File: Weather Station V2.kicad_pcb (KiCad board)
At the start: 4 copper layers, 123.5 x 67.3 mm, 66 parts, among them J1 SOLAR IN, J10 SP13 Socket, J2 18650, J3 Battery_AUX, J4 Conn_01x08_Socket, J5 Conn_01x08_Socket, J6 USB_C, J7 RYLR998, J8 Breakout, J9 SP13 Socket, Q1 AO4842, Q2 DMP2240UDM-7, Q3 BC547, SW1 LED_ENABLE, SW2 EN/RST, SW3 BOOT, SW4 POWER_SELECT, SW6 POWER, U1 TP4056, U2 DW01A, U3 LDL1117S33R, U4 MT3608, U5 ESP32-S3-WROOM-1U, U7 USBLC6-2SC6

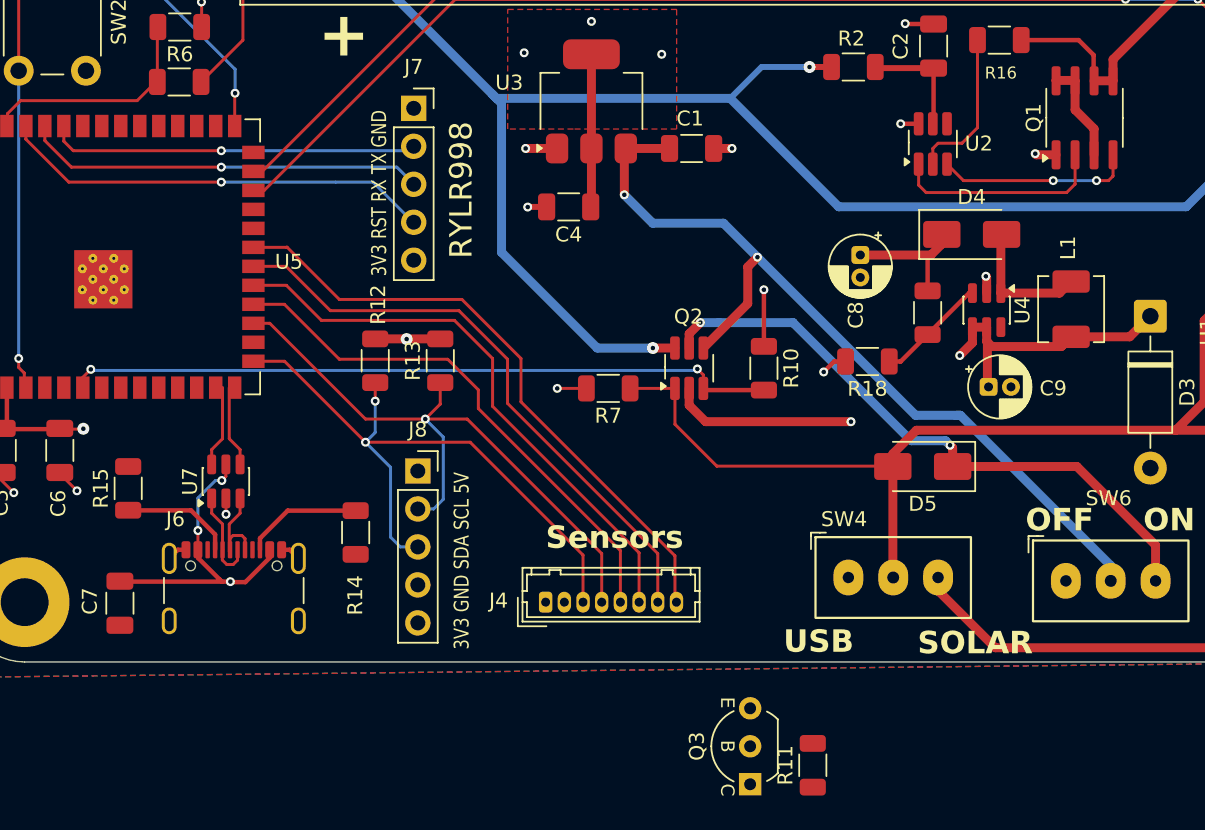
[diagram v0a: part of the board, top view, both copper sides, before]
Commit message: - Connected open collector mosfet driver to 5V reg - Re-routed tracks related to NMOS
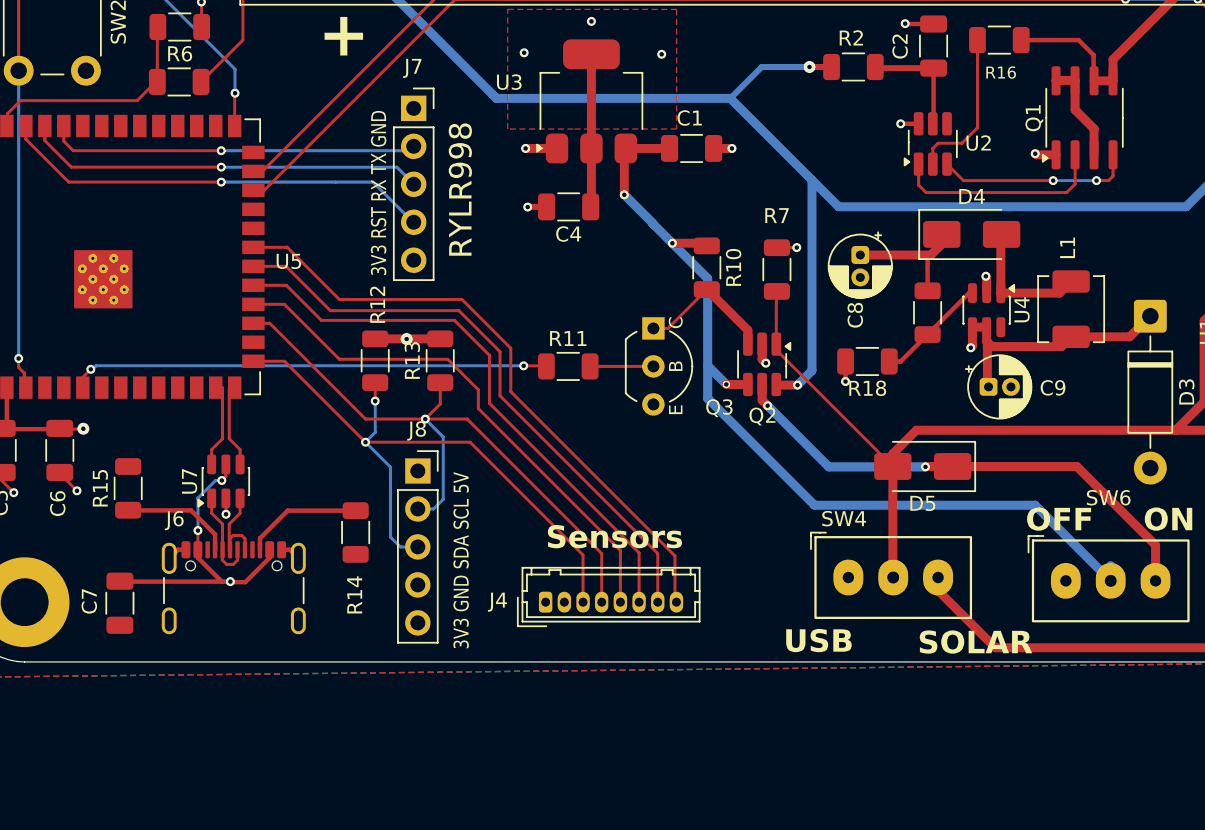
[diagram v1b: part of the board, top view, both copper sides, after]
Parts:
- moved R11 31.3 mm to (128.8, 105.2), turned to 0 degrees
- moved Q3 31.2 mm to (134.5, 102.6), turned to -90 degrees
- moved R7 13.8 mm to (142.8, 98.7), turned to 90 degrees
- moved R10 7.73 mm to (138.1, 98.6)
- moved Q2 4.89 mm to (141.8, 105.0), turned to -90 degrees
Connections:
- net /~{SENSOR_EN} renamed /SENSOR_EN
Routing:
- net /SENSOR_EN: track 47.7 -> 32.0 mm
- net /BAT+: track 166.7 -> 157.1 mm
- net Net-(Q2B-G): track 0.00 -> 9.45 mm
- net Net-(D5-K): track 41.8 -> 33.8 mm
- net Net-(D3-K): track 40.6 -> 33.8 mm
- net /Vin: track 74.3 -> 68.0 mm
- net Net-(Q3-B): track 0.00 -> 4.29 mm
- net /Battery_SW: track 61.5 -> 60.6 mm, vias 2 -> 3
- net +5V: track 55.6 -> 54.9 mm
- net GND: track 37.5 -> 37.0 mm
- net +3V3: vias 8 -> 7

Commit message: - Fixed Back to Back mosfet (now the follow DW01A datasheet) - Connected STDBY and CHRG leds to Vin - Removed STDBY and CHRG mcu monitoring (risk of frying the pins) - TP4056 Vcc cap 0.1 to 10 uf - Added BAT+ coupling cap STDBY and CHRG
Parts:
- added C10: 10u, Capacitor_SMD:C_1206_3216Metric, F.Cu at (180.5, 100.5)
- C3: value 0.1u -> 10u
- R4, R5: value 330 -> 1k
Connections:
- Q1 pad 3: Net-(Q1B-S2) -> /BAT-
- Q1 pad 5: /BAT- -> Net-(Q1A-D1-Pad7)
- Q1 pad 6: /BAT- -> Net-(Q1A-D1-Pad7)
- Q1 pad 7: Net-(Q1B-S2) -> Net-(Q1A-D1-Pad7)
- Q1 pad 8: Net-(Q1B-S2) -> Net-(Q1A-D1-Pad7)
- R4 pad 2: /~{STDBY} -> Net-(U1-~{STDBY})
- R5 pad 2: /~{CHRG} -> Net-(U1-~{CHRG})
- SW1 pad 1: +3V3 -> /Vin
- U1 pad 6: /~{STDBY} -> Net-(U1-~{STDBY})
- U1 pad 7: /~{CHRG} -> Net-(U1-~{CHRG})
- U5 pad 24: /~{STDBY} -> unconnected-(U5-IO47-Pad24)
- U5 pad 25: /~{CHRG} -> unconnected-(U5-IO48-Pad25)
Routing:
- net /~{CHRG}: track 101.1 -> 0.00 mm, vias 2 -> 0
- net /~{STDBY}: track 98.8 -> 0.00 mm, vias 4 -> 0
- net +3V3: track 73.1 -> 26.8 mm
- net Net-(U1-~{CHRG}): track 0.00 -> 17.1 mm
- net /Vin: track 68.0 -> 81.7 mm
- net Net-(U1-~{STDBY}): track 0.00 -> 13.3 mm
- net /BAT-: track 41.7 -> 48.9 mm
- net Net-(Q1B-S2): track 6.78 -> 0.00 mm
- net Net-(Q1A-D1-Pad7): track 0.00 -> 3.85 mm
- net /BAT+: track 157.1 -> 160.7 mm
- net GND: track 37.0 -> 37.9 mm, vias 19 -> 20

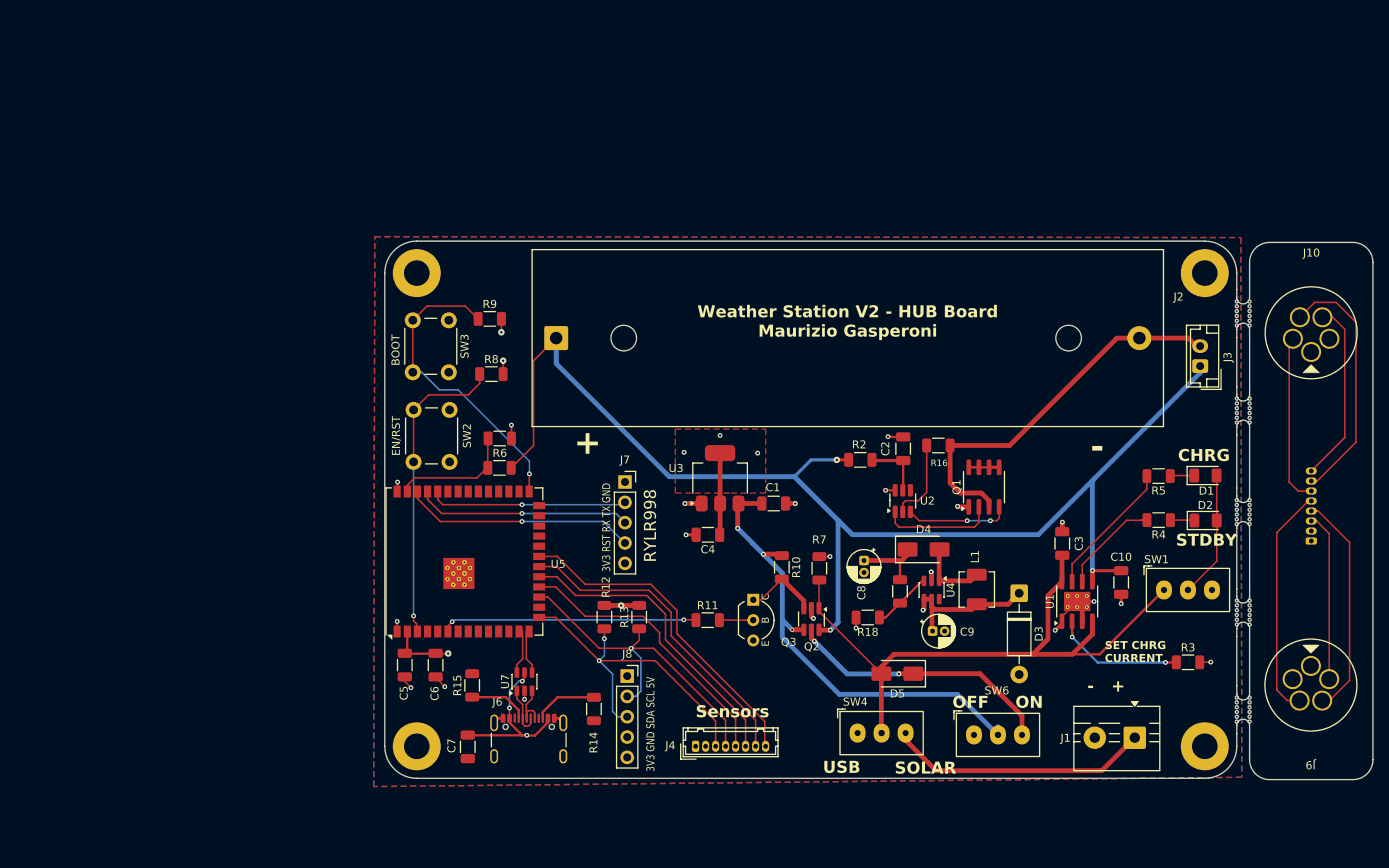
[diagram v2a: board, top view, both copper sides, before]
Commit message: - Changed revision to Rev 3 - Removed Production Folder - Changed DW01A Resistor value to match datasheet
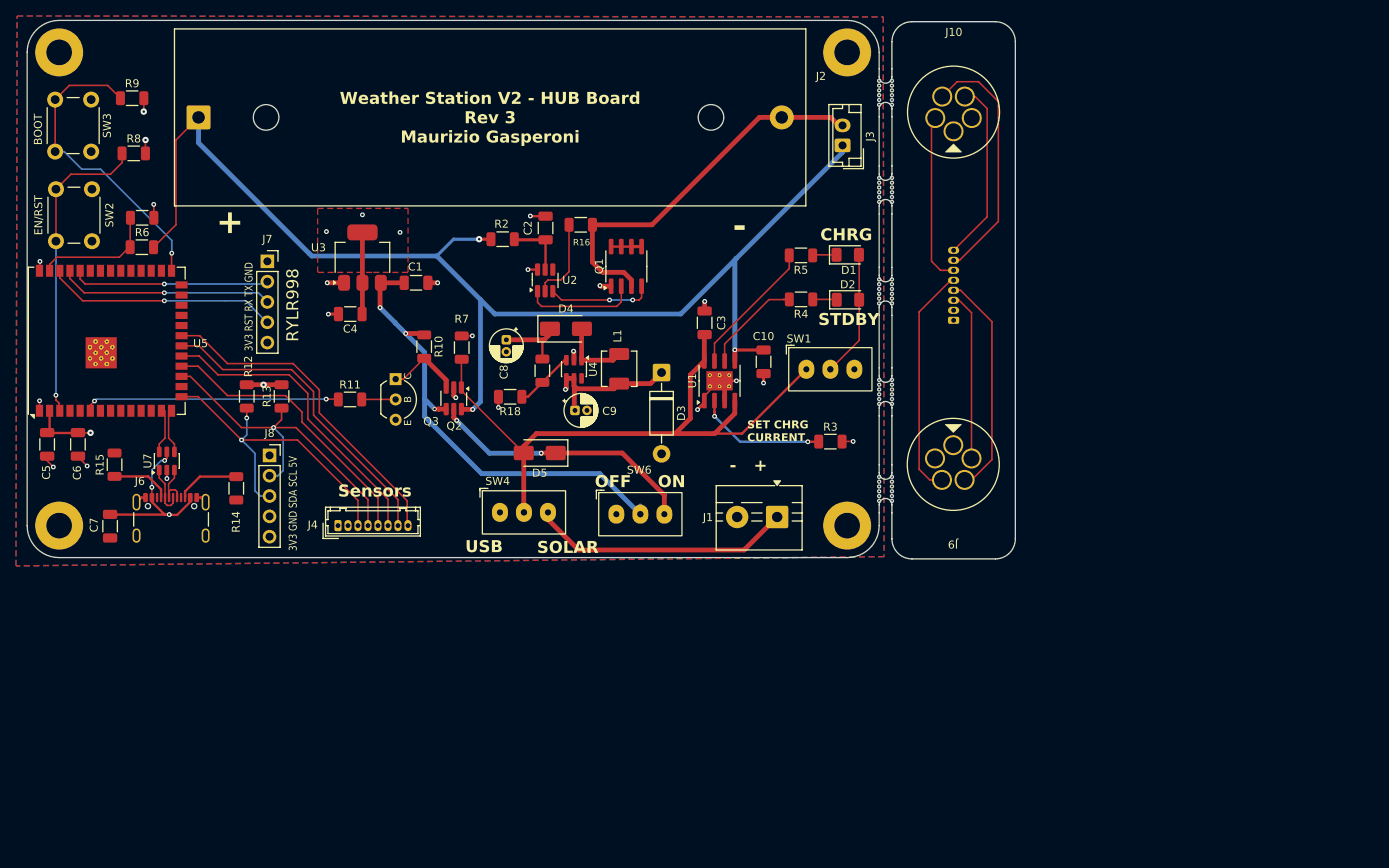
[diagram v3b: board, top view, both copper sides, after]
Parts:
- R16: value 5K -> 2K
- R2: value 100 -> 470
- moved D1 52.5 mm to (146.4, 59.5)
- moved H3 52.5 mm to (146.3, 34.2)
- moved H4 52.5 mm to (146.3, 93.4)
- moved J1 52.5 mm to (137.5, 92.3)
- moved J4 52.5 mm to (82.6, 93.4)
- moved J6 52.5 mm to (61.8, 93.5)
- moved J9 52.5 mm to (159.5, 85.7)
- moved M2 52.5 mm to (150.3, 91.8)
- moved M4 52.5 mm to (150.3, 54.4)
- moved Q3 52.5 mm to (89.8, 75.1)
- moved R1 52.5 mm to (58.1, 58.6)
- moved R10 52.5 mm to (93.4, 71.0)
- moved R2 52.5 mm to (103.2, 57.6)
- moved R3 52.5 mm to (144.2, 82.9)
- moved R5 52.5 mm to (140.5, 59.6)
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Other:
- outline, holes or cut-outs redrawn
- board text added: "Weather Station V2 - HUB Board Rev 3 Maurizio Gasperoni"
- board text removed: "Weather Station V2 - HUB Board Maurizio Gasperoni"

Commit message: - Localized Libraries
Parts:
- C1, C10, C2, C3, C4, C5, C6, C7: footprint Capacitor_SMD:C_1206_3216Metric -> FootprintsLib:C_1206_3216Metric
- C8, C9: footprint Capacitor_THT:CP_Radial_D4.0mm_P1.50mm -> FootprintsLib:CP_Radial_D4.0mm_P1.50mm
- D1, D2: footprint LED_SMD:LED_1206_3216Metric -> FootprintsLib:LED_1206_3216Metric
- D3: footprint Diode_THT:D_DO-41_SOD81_P10.16mm_Horizontal -> FootprintsLib:D_DO-41_SOD81_P10.16mm_Horizontal
- D4, D5: footprint Diode_SMD:D_SMA -> FootprintsLib:D_SMA
- H1, H2, H3, H4: footprint PCM_SL_Mechanical:MountingHole_3.2mm_Pad -> FootprintsLib:MountingHole_3.2mm_Pad
- J1: footprint TerminalBlock:TerminalBlock_MaiXu_MX126-5.0-02P_1x02_P5.00mm -> FootprintsLib:TerminalBlock_MaiXu_MX126-5.0-02P_1x02_P5.00mm
- J10, J9: footprint SP13_5pin_holes:SP13_5pin_holes -> FootprintsLib:SP13_5pin_holes
- J2: footprint Battery:BatteryHolder_MPD_BH-18650-PC -> FootprintsLib:BatteryHolder_MPD_BH-18650-PC
- J3: footprint Connector_JST:JST_EH_B2B-EH-A_1x02_P2.50mm_Vertical -> FootprintsLib:JST_EH_B2B-EH-A_1x02_P2.50mm_Vertical
- J4, J5: footprint Connector_Hirose:Hirose_DF13-08P-1.25DSA_1x08_P1.25mm_Vertical -> FootprintsLib:Hirose_DF13-08P-1.25DSA_1x08_P1.25mm_Vertical
- J6: footprint Connector_USB:USB_C_Receptacle_GCT_USB4105-xx-A_16P_TopMnt_Horizontal -> FootprintsLib:USB_C_Receptacle_GCT_USB4105-xx-A_16P_TopMnt_Horizontal
- J7, J8: footprint Connector_PinSocket_2.54mm:PinSocket_1x05_P2.54mm_Vertical -> FootprintsLib:PinSocket_1x05_P2.54mm_Vertical
- L1: footprint Inductor_SMD:L_APV_APH0420 -> FootprintsLib:L_APV_APH0420
- Q1: footprint Package_SO:SOIC-8_3.9x4.9mm_P1.27mm -> FootprintsLib:SOIC-8_3.9x4.9mm_P1.27mm
- Q2, U2: footprint Package_TO_SOT_SMD:SOT-23-6_Handsoldering -> FootprintsLib:SOT-23-6_Handsoldering
- Q3: footprint PCM_Package_TO_SOT_THT_AKL:TO-92_Inline_Wide_CBE -> FootprintsLib:TO-92_Inline_Wide_CBE
- R1, R10, R11, R12, R13, R14, R15, R16, R17, R18, R2, R3, R4, R5, R6, R7, R8, R9: footprint Resistor_SMD:R_1206_3216Metric -> FootprintsLib:R_1206_3216Metric
- SW1, SW4, SW6: footprint PCM_SL_Devices:Slide_Switch_SPDT_P3mm_10x5x10mm -> FootprintsLib:Slide_Switch_SPDT_P3mm_10x5x10mm
- SW2, SW3: footprint Button_Switch_THT:SW_PUSH_6mm -> FootprintsLib:SW_PUSH_6mm
- U1: footprint Package_SO:SOIC-8-1EP_3.9x4.9mm_P1.27mm_EP2.41x3.3mm_ThermalVias -> FootprintsLib:SOIC-8-1EP_3.9x4.9mm_P1.27mm_EP2.41x3.3mm_ThermalVias
- U3: footprint Package_TO_SOT_SMD:SOT-223-3_TabPin2 -> FootprintsLib:SOT-223-3_TabPin2
- U4, U7: footprint Package_TO_SOT_SMD:SOT-23-6 -> FootprintsLib:SOT-23-6
- U5: footprint RF_Module:ESP32-S3-WROOM-1U -> FootprintsLib:ESP32-S3-WROOM-1U
